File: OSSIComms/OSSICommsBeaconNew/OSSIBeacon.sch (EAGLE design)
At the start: 21 parts, among them U10 MAX6369, U12 TPS73233, U3 MAX890L, U4 OPA2347, U7 TPS3838, X2 DF13-10PA

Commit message: OSSI New Beacon Board Circuit 90% done
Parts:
- added C10, C11, C14, C15, C16, C22, C25, C32, C4, C5, C6, C8, C9: (no value), OSSI:C0603(1608)
- added C17, C18: 12.5pF, OSSI:C0603(1608)
- added C2, C24, C29, C31: 100nF, OSSI:C0603(1608)
- added C23: 1uF, OSSI:C0603(1608)
- added C26: 1uF,0805, OSSI:C0805(2012)
- added C27, C28, C76: 10nF, OSSI:C0603(1608)
- added C3: 1uF, 0805, OSSI:C0805(2012)
- added C30: 10uF,1210, OSSI:C1210(3225)-GCM32
- added C62: 22nF, OSSI:C0603(1608)
- added C7: 1uF 0805, OSSI:C0805(2012)
- added C77: 22pF, OSSI:C0603(1608)
- added F1: LFCN-160, OSSI:LFCN-160
- added L1, L2: 470nH, 1008 size, OSSI:L1008(2502)
- added L10: 10nH, OSSI:L0603(1608)
- added L3, L4: (no value), OSSI:L0603(1608)
- added LED1: (no value), SparkFun:LED0603
- added Q2: NX-3215, OSSI:NX-3215
- added R1, R12, R34: 100k, OSSI:R0603(1608)
- added R13: 1.6k, OSSI:R0603(1608)
- added R16: 4.7k, OSSI:R0603(1608)
- added R2, R3: (no value), OSSI:R0603(1608)
- added R25: 3.6k, OSSI:R0603(1608)
- added R33: 1k, OSSI:R0603(1608)
- added R4: 0, OSSI:R0603(1608)
- added R63, R67: 250, OSSI:R0603(1608)
- added R68, R71: 10k, OSSI:R0603(1608)
- added TCXO1: 19.2MHz, OSSI:TCXO-M532
- added TR3: FDV301N, OSSI:FDV301N
- added U1: MSP430F2132, OSSI:MSP430F2132
- added U2: ADF7012, OSSI:ADF7012
- added U5: ADL5530, OSSI:ADL5530
- added U6: MAX890L, OSSI:MAX890L
- added X1: RFCON-MCX-R/A, OSSI:RFCON-MCX-R/A
- added X5: JTAG10PINMINI-H, OSSI:JTAG10PINMINI-H
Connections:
- new net BEACON_CE: U1.18, U2.CE
- new net BEACON_DATA: U1.24, U2.TXDATA
- new net BEACON_MUXOUT: U1.22, U2.MUXOUT
- new net BEACON_RFOUT: C25.2, C27.1, L4.2
- new net BEACON_SCLK: U1.21, U2.CLK
- new net BEACON_SDATA: U1.20, U2.DATA
- new net BEACON_SLE: U1.19, U2.LE
- new net BEACON_TCXO: C77.2, U2.OSC1
- new net BEACON_TXCLK: U1.23, U2.TXCLK
- new net N$1: R33.1, U1.14
- new net N$10: R67.2, U1.13
- new net N$11: R22.1
- new net N$12: U1.10, U10.P$1
- new net N$13: U1.11
- new net N$14: L10.1, U2.L2
- new net N$15: L10.2, U2.L1
- new net N$16: C62.1, C7.2, U2.CREG2
- new net N$17: C62.2, U2.CVCO
- new net N$18: R25.2, U2.RSET
- new net N$19: C23.1, R12.1, TR3.D, U6.P$3
- new net N$2: U1.27, X5.3
- new net N$20: C5.1, R3.1
- new net N$21: R13.2, U6.P$5
- new net N$23: C15.2, L1.2, U2.RFOUT
- new net N$24: C4.1, R2.1, U2.VCOIN
- new net N$25: C3.2, U2.CREG1
- new net N$26: C5.2, C6.2, R2.2, U2.CPOUT
- new net N$27: C8.1, C9.1, L1.1, R4.2, U2.DVDD_2
- new net N$28: C27.2, U5.2
- new net N$29: C15.1, C16.2, L3.1
- new net N$3: U1.26, X5.5
- new net N$30: C28.1, L2.2, U5.7
- new net N$31: R16.1, X5.10
- new net N$34: C28.2, F1.P$1
- new net N$35: C32.1, F1.P$3
- new net N$36: C22.2, L3.2, L4.1
- new net N$37: C32.2, X1.1
- new net N$4: U1.25, X5.7
- new net N$5: C17.1, Q2.2, U1.5
- new net N$6: C18.1, Q2.1, U1.6
- new net N$69: C77.1, TCXO1.P$3
- new net N$7: LED1.A, R33.2
- new net N$8: U1.28, X5.1
- new net N$9: R63.2, U1.12
- new net PA_-FAULT: R34.1, U1.3, U6.P$8
- new net PA_ON: R1.2, TR3.G, U1.17
- new net RXD: U1.16
- new net TXD: U1.15
- new net VCCRF: C10.1, C11.1, C14.1, C76.1, R4.1, TCXO1.P$4, U2.DVDD_1
- net 3.3VBEACON: now also C2.1, R34.2, R68.2, R71.2, U1.2, X5.4
- net ADC0: now also U1.8
- net ADC1: now also U1.9
- net GND: now also C10.2, C11.2, C14.2, C16.1, C17.2, C18.2, C2.2, C22.1, C23.2, C24.2, C25.1, C26.2, C29.2, C3.1, C30.2, C31.2, C4.2, C6.1, C7.1, C76.2, C8.2, C9.2, F1.P$2, F1.P$4, LED1.C, R1.1, R13.1, R25.1, R3.2, TCXO1.P$1, TCXO1.P$2, TR3.S, U1.4, U2.AGND, U2.DGND, U2.RFGND, U5.1, U5.3, U5.4, U5.5, U5.6, U5.8, U6.P$4, X1.2, X1.3, X1.4, X1.5, X5.9
- net I2CSEC_SCL: now also R67.1, R71.1
- net I2CSEC_SDA: now also R63.1, R68.1
- net RESETBEACON: now also R16.2, U1.7
- net VBEACON_PA: now also C24.1, C26.1, C29.1, C30.1, C31.1, L2.1, U6.P$6, U6.P$7; no longer R22.1
- net VBUS: now also R12.2, U6.P$1, U6.P$2
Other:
- note added: "Capacitors!!!!!"
- note added: "PA Off by default"
- note added: "Sine Wave outout TCXO to OSC1 pin with series capacitor"
- note added: "use board's power"
- moved on the sheet: C1, U10

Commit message: New Beacon board updating
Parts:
- added H1, H2, H3, H4: MOUNT-PAD-ROUND3.2, OSSI:MOUNT-PAD-ROUND3.2
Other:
- moved on the sheet: C26, C30
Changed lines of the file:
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@@
 <part name="GND33" library="OSSI" deviceset="GND" device=""/>
 <part name="GND34" library="OSSI" deviceset="GND" device=""/>
+<part name="H1" library="OSSI" deviceset="MOUNT-PAD-ROUND" device="3.2"/>
+<part name="H2" library="OSSI" deviceset="MOUNT-PAD-ROUND" device="3.2"/>
+<part name="H3" library="OSSI" deviceset="MOUNT-PAD-ROUND" device="3.2"/>
+<part name="H4" library="OSSI" deviceset="MOUNT-PAD-ROUND" device="3.2"/>
 </parts>
 <sheets>
@@
 <instance part="R1" gate="G$1" x="86.36" y="185.42" rot="R90"/>
 <instance part="GND7" gate="1" x="86.36" y="175.26"/>
-<instance part="C26" gate="G$1" x="180.34" y="203.2"/>
-<instance part="GND39" gate="1" x="180.34" y="190.5"/>
-<instance part="C30" gate="G$1" x="190.5" y="203.2"/>
+<instance part="C26" gate="G$1" x="180.34" y="152.4" rot="R90"/>
+<instance part="GND39" gate="1" x="170.18" y="187.96"/>
+<instance part="C30" gate="G$1" x="180.34" y="165.1" rot="R90"/>
 <instance part="L2" gate="G$1" x="167.64" y="116.84"/>
 <instance part="C27" gate="G$1" x="116.84" y="104.14" rot="R90"/>
@@
 <instance part="GND33" gate="1" x="198.12" y="91.44"/>
 <instance part="GND34" gate="1" x="198.12" y="116.84" rot="R180"/>
+<instance part="H1" gate="G$1" x="20.32" y="243.84"/>
+<instance part="H2" gate="G$1" x="20.32" y="231.14"/>
+<instance part="H3" gate="G$1" x="20.32" y="218.44"/>
+<instance part="H4" gate="G$1" x="20.32" y="205.74"/>
 </instances>
 <busses>
@@
 <segment>
 <pinref part="GND39" gate="1" pin="GND"/>
-<pinref part="C26" gate="G$1" pin="2"/>
-<wire x1="180.34" y1="193.04" x2="180.34" y2="198.12" width="0.1524" layer="91"/>
-<pinref part="C30" gate="G$1" pin="2"/>
-<wire x1="190.5" y1="198.12" x2="190.5" y2="193.04" width="0.1524" layer="91"/>
-<wire x1="190.5" y1="193.04" x2="180.34" y2="193.04" width="0.1524" layer="91"/>
-<junction x="180.34" y="193.04"/>
 <pinref part="C24" gate="G$1" pin="2"/>
 <wire x1="170.18" y1="193.04" x2="170.18" y2="198.12" width="0.1524" layer="91"/>
-<wire x1="180.34" y1="193.04" x2="170.18" y2="193.04" width="0.1524" layer="91"/>
+<wire x1="170.18" y1="190.5" x2="170.18" y2="193.04" width="0.1524" layer="91"/>
 </segment>
 <segment>
@@
 <wire x1="190.5" y1="139.7" x2="193.04" y2="139.7" width="0.1524" layer="91"/>
 <junction x="190.5" y="139.7"/>
+<pinref part="C30" gate="G$1" pin="2"/>
+<wire x1="185.42" y1="165.1" x2="190.5" y2="165.1" width="0.1524" layer="91"/>
+<wire x1="190.5" y1="165.1" x2="190.5" y2="152.4" width="0.1524" layer="91"/>
+<pinref part="C26" gate="G$1" pin="2"/>
+<wire x1="190.5" y1="152.4" x2="190.5" y2="139.7" width="0.1524" layer="91"/>
+<wire x1="185.42" y1="152.4" x2="190.5" y2="152.4" width="0.1524" layer="91"/>
+<junction x="190.5" y="152.4"/>
 </segment>
 <segment>
@@
 <junction x="170.18" y="208.28"/>
 <label x="198.12" y="208.28" size="1.778" layer="95" xref="yes"/>
-<pinref part="C26" gate="G$1" pin="1"/>
-<wire x1="180.34" y1="205.74" x2="180.34" y2="208.28" width="0.1524" layer="91"/>
-<junction x="180.34" y="208.28"/>
-<pinref part="C30" gate="G$1" pin="1"/>
-<wire x1="190.5" y1="205.74" x2="190.5" y2="208.28" width="0.1524" layer="91"/>
-<junction x="190.5" y="208.28"/>
 </segment>
 <segment>
 <pinref part="L2" gate="G$1" pin="1"/>
 <wire x1="167.64" y1="124.46" x2="167.64" y2="132.08" width="0.1524" layer="91"/>
-<label x="167.64" y="144.78" size="1.778" layer="95" rot="R90" xref="yes"/>
+<label x="167.64" y="167.64" size="1.778" layer="95" rot="R90" xref="yes"/>
 <pinref part="C29" gate="G$1" pin="1"/>
 <wire x1="167.64" y1="132.08" x2="167.64" y2="139.7" width="0.1524" layer="91"/>
-<wire x1="167.64" y1="139.7" x2="167.64" y2="144.78" width="0.1524" layer="91"/>
+<wire x1="167.64" y1="139.7" x2="167.64" y2="152.4" width="0.1524" layer="91"/>
+<wire x1="167.64" y1="152.4" x2="167.64" y2="165.1" width="0.1524" layer="91"/>
+<wire x1="167.64" y1="165.1" x2="167.64" y2="167.64" width="0.1524" layer="91"/>
 <wire x1="177.8" y1="132.08" x2="167.64" y2="132.08" width="0.1524" layer="91"/>
 <junction x="167.64" y="132.08"/>
@@
 <wire x1="177.8" y1="139.7" x2="167.64" y2="139.7" width="0.1524" layer="91"/>
 <junction x="167.64" y="139.7"/>
-</segment>
-</net>
+<pinref part="C26" gate="G$1" pin="1"/>
+<wire x1="177.8" y1="152.4" x2="167.64" y2="152.4" width="0.1524" layer="91"/>
+<junction x="167.64" y="152.4"/>
+<pinref part="C30" gate="G$1" pin="1"/>
+<wire x1="177.8" y1="165.1" x2="167.64" y2="165.1" width="0.1524" layer="91"/>
+<junction x="167.64" y="165.1"/>
+</segment>
+</net>

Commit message: OSSI New Beacon Almost done
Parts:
- added C33, C36: 10pF, OSSI:C0603(1608)
- added C37: 10nF, OSSI:C0603(1608)
- added C38: 100nF, OSSI:C0603(1608)
- added L11: 0 Ohm, OSSI:L0805(2012)
- added Q1: CX5032SB, OSSI:CX5032SB
- added U$1: OSSILOGORECT, OSSI:OSSILOGORECT
- added X3: MOLEX-22-05-7035, OSSI:MOLEX-22-05-7035
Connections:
- removed net I2CSEC_SCL: R67.1, R71.1, X2.4
- removed net I2CSEC_SDA: R63.1, R68.1, X2.5
- removed net N$11: R22.1
- new net BEACON_ADCIN: R22.1, X2.5
- new net BEACON_CWCONTROL: X2.4
- new net N$41: C33.1, Q1.3, U2.OSC2
- net 3.3VBEACON: now also C37.1, L11.1
- net BEACON_SCL: now also R67.1, R71.1
- net BEACON_SDA: now also R63.1, R68.1
- net BEACON_TCXO: now also C36.1, Q1.1
- net GND: now also C33.2, C36.2, C37.2, C38.2, Q1.2, Q1.4, X3.1
- net N$1: now also U1.11; no longer U1.14
- net N$13: now also U1.14; no longer U1.11
- net RXD: now also X3.3
- net TXD: now also X3.2
- net VCCRF: now also C38.1, L11.2
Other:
- note added: "DIGITAL / RF POWER CHOKE"
- moved on the sheet: LED1, R33

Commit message: OSSI New Beacon layout done
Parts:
- removed U12: TPS73233, OSSI:TPS73233
- added C39: 100nF, OSSI:C0603(1608)
- added D1: BAT54S, OSSI:BAT54S
- added D2, D3: TPD1E10B06, OSSI:TPD1E10B06
- added JP1: (no value), OSSI:JP1Q
- added R5, R6, R7, R8: 4.7k, OSSI:R0603(1608)
- added U8: TPS76933, OSSI:TPS76933
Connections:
- new net N$11: R7.2, U1.16
- new net N$39: R6.2, U1.15
- net 3.3VBEACON: now also D1.C2, U8.5; no longer U12.5
- net BEACON_ADCIN: now also D3.1
- net BEACON_CWCONTROL: now also D2.1, R5.2, R8.1
- net GND: now also C39.2, D1.A1, D2.2, D3.2, JP1.1, R8.2, U8.2, U8.3; no longer U12.2
- net N$13: now also C39.1, D1.C1A2, R5.1
- net N$666: now also U8.1; no longer U12.1, U12.3
- net N$7: now also JP1.2
- net RXD: now also R7.1; no longer U1.16
- net TXD: now also R6.1; no longer U1.15
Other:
- note added: "Check TVS influences on OpAmp Input"
- note added: "Pull Down resistor!!"

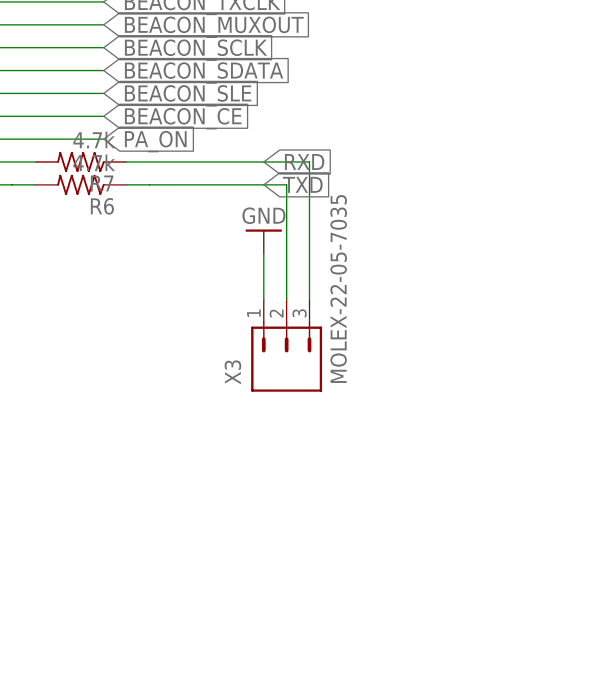
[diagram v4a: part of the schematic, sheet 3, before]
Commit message: I2C Testboard gerber done / New Beacon gerber done
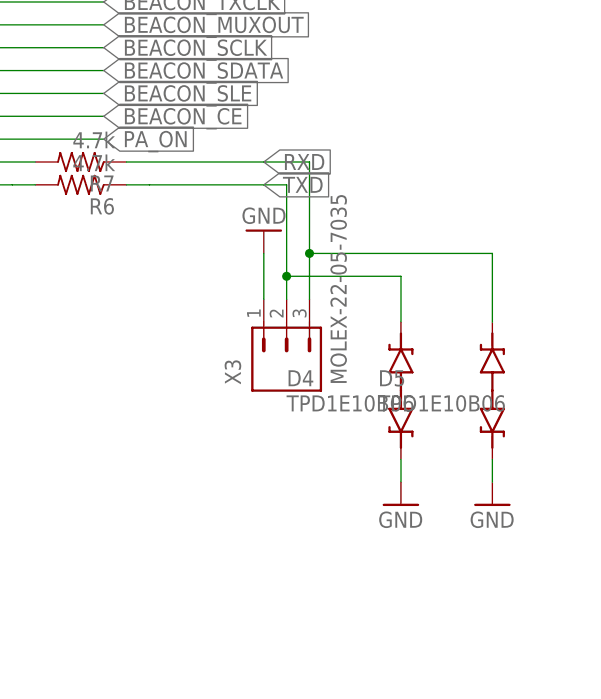
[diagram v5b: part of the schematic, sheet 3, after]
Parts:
- added D4, D5: TPD1E10B06, OSSI:TPD1E10B06
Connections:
- net GND: now also D4.2, D5.2
- net RXD: now also D5.1
- net TXD: now also D4.1
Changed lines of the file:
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@@
 <part name="D3" library="OSSI" deviceset="TPD1E10B06" device=""/>
 <part name="GND47" library="OSSI" deviceset="GND" device=""/>
+<part name="D4" library="OSSI" deviceset="TPD1E10B06" device=""/>
+<part name="D5" library="OSSI" deviceset="TPD1E10B06" device=""/>
+<part name="GND48" library="OSSI" deviceset="GND" device=""/>
+<part name="GND49" library="OSSI" deviceset="GND" device=""/>
 </parts>
 <sheets>
@@
 <instance part="D3" gate="G$1" x="17.78" y="160.02" rot="R270"/>
 <instance part="GND47" gate="1" x="5.08" y="160.02" rot="R270"/>
+<instance part="D4" gate="G$1" x="330.2" y="88.9"/>
+<instance part="D5" gate="G$1" x="340.36" y="88.9"/>
+<instance part="GND48" gate="1" x="330.2" y="76.2"/>
+<instance part="GND49" gate="1" x="340.36" y="76.2"/>
 </instances>
 <busses>
@@
 <pinref part="D3" gate="G$1" pin="2"/>
 <wire x1="7.62" y1="160.02" x2="10.16" y2="160.02" width="0.1524" layer="91"/>
+</segment>
+<segment>
+<pinref part="GND48" gate="1" pin="GND"/>
+<pinref part="D4" gate="G$1" pin="2"/>
+<wire x1="330.2" y1="78.74" x2="330.2" y2="81.28" width="0.1524" layer="91"/>
+</segment>
+<segment>
+<pinref part="GND49" gate="1" pin="GND"/>
+<pinref part="D5" gate="G$1" pin="2"/>
+<wire x1="340.36" y1="78.74" x2="340.36" y2="81.28" width="0.1524" layer="91"/>
 </segment>
 </net>
@@
 <wire x1="302.26" y1="111.76" x2="314.96" y2="111.76" width="0.1524" layer="91"/>
 <wire x1="314.96" y1="111.76" x2="317.5" y2="111.76" width="0.1524" layer="91"/>
-<wire x1="317.5" y1="111.76" x2="317.5" y2="99.06" width="0.1524" layer="91"/>
+<wire x1="317.5" y1="111.76" x2="317.5" y2="101.6" width="0.1524" layer="91"/>
 <pinref part="R6" gate="G$1" pin="1"/>
+<wire x1="317.5" y1="101.6" x2="317.5" y2="99.06" width="0.1524" layer="91"/>
 <wire x1="299.72" y1="111.76" x2="302.26" y2="111.76" width="0.1524" layer="91"/>
+<pinref part="D4" gate="G$1" pin="1"/>
+<wire x1="317.5" y1="101.6" x2="330.2" y2="101.6" width="0.1524" layer="91"/>
+<wire x1="330.2" y1="101.6" x2="330.2" y2="96.52" width="0.1524" layer="91"/>
+<junction x="317.5" y="101.6"/>
 </segment>
 </net>
@@
 <wire x1="299.72" y1="114.3" x2="314.96" y2="114.3" width="0.1524" layer="91"/>
 <wire x1="314.96" y1="114.3" x2="320.04" y2="114.3" width="0.1524" layer="91"/>
-<wire x1="320.04" y1="114.3" x2="320.04" y2="99.06" width="0.1524" layer="91"/>
+<wire x1="320.04" y1="114.3" x2="320.04" y2="104.14" width="0.1524" layer="91"/>
 <pinref part="R7" gate="G$1" pin="1"/>
-</segment>
-</net>
+<pinref part="D5" gate="G$1" pin="1"/>
+<wire x1="320.04" y1="104.14" x2="320.04" y2="99.06" width="0.1524" layer="91"/>
+<wire x1="320.04" y1="104.14" x2="340.36" y2="104.14" width="0.1524" layer="91"/>
+<wire x1="340.36" y1="104.14" x2="340.36" y2="96.52" width="0.1524" layer="91"/>
+<junction x="320.04" y="104.14"/>
+</segment>
+</net>

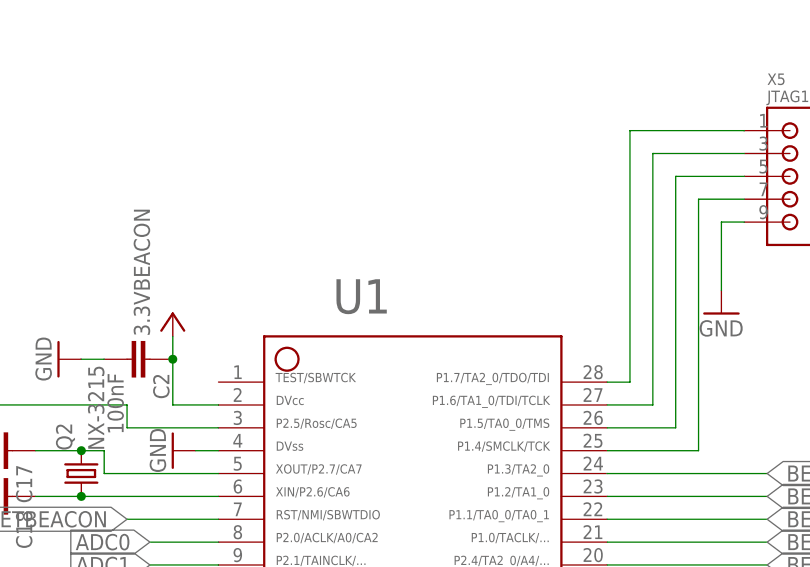
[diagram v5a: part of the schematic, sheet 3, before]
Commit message: 2132 based LED controller being made / related lbr updated
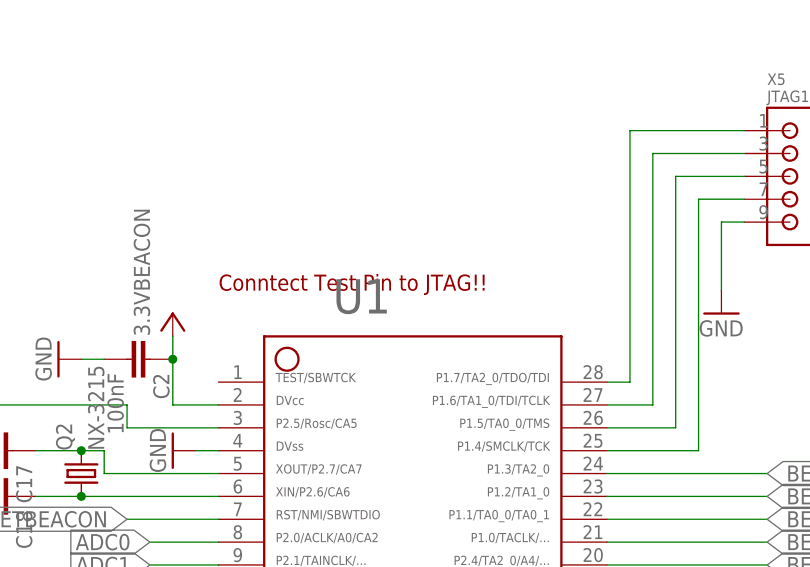
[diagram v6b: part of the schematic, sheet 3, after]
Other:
- note added: "Conntect Test Pin to JTAG!!"
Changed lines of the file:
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@@
 <text x="231.14" y="15.24" size="1.778" layer="94">Pull Down resistor!!</text>
 <text x="10.16" y="193.04" size="1.778" layer="94">Check TVS influences on OpAmp Input</text>
+<text x="236.22" y="154.94" size="1.778" layer="94">Conntect Test Pin to JTAG!!</text>
 </plain>
 <instances>
